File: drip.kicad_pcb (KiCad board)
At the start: 2 copper layers, 119.4 x 115.6 mm, 103 parts, among them J1 ISP, J2 2xAA Battery Holder, Q1 2n2907, Q2 2n2907, Q3 2n2907, Q4 2n2907, Q5 2n2907, Q6 2n2907, Q7 2n2907, Q8 2n2907, Q9 2n2222, SW1 Bin, SW10 Recall, SW11 D, SW12 A, SW13 7, SW14 4, SW15 1, SW16 0, SW17 Hex, SW18 E, SW19 B, SW2 Store, SW20 8, SW21 5, SW22 2, SW23 Decimal, SW24 Oct, SW25 F, SW26 C, SW27 9, SW28 6, SW29 3, SW3 Shift, SW30 +/-, SW31 Clear, SW32 K, SW33 Div, SW34 Mul, SW35 Minus, SW36 Plus, SW37 Enter, SW4 1'sCompl, SW5 Or, SW6 And, SW7 Xor, SW8 Clear Entry, SW9 Dec, U1 74HC138, U2 5641AS-4Digit-7Segment, U3 5641AS-4Digit-7Segment, U4 MSP430G2553IN20, U5 74HC251, U6 74HC138, U7 74HC595, U8 XC6372A331PR-G

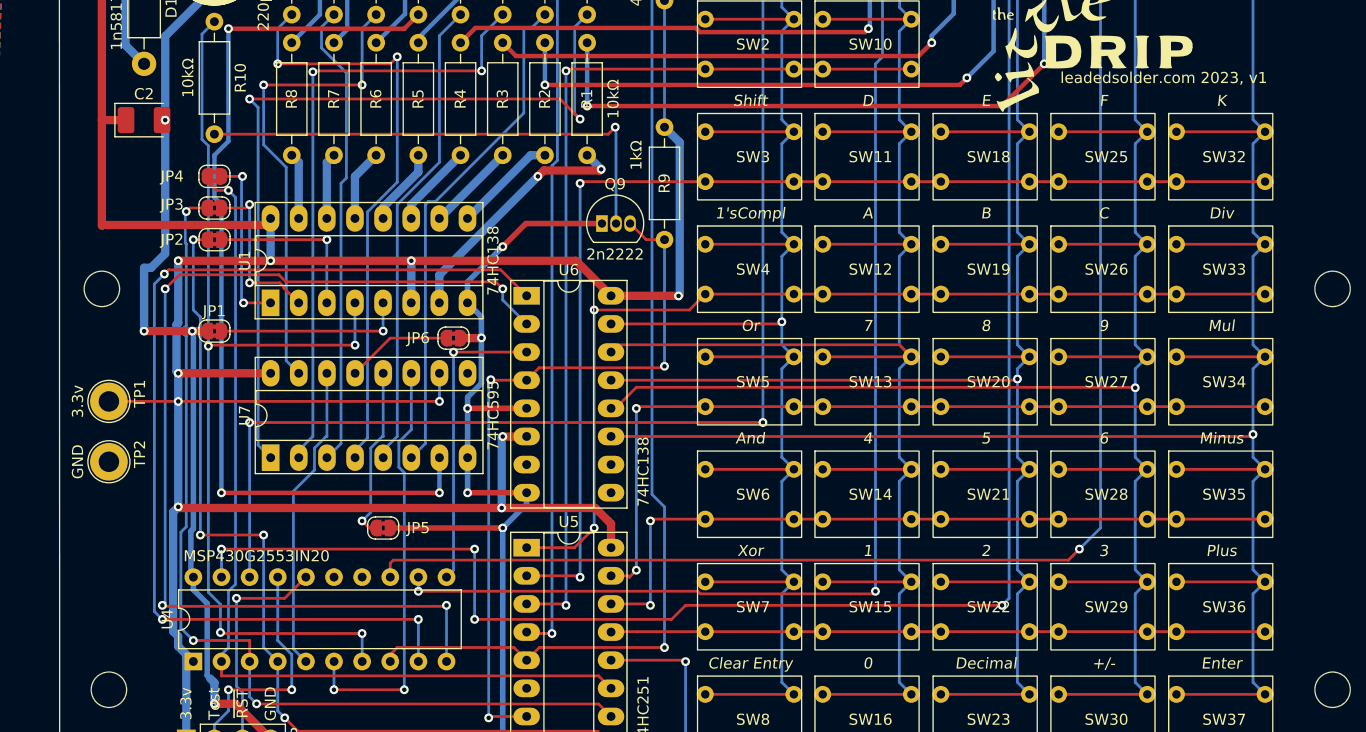
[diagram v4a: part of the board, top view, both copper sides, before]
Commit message: Reset pullup, move test hooks further apart
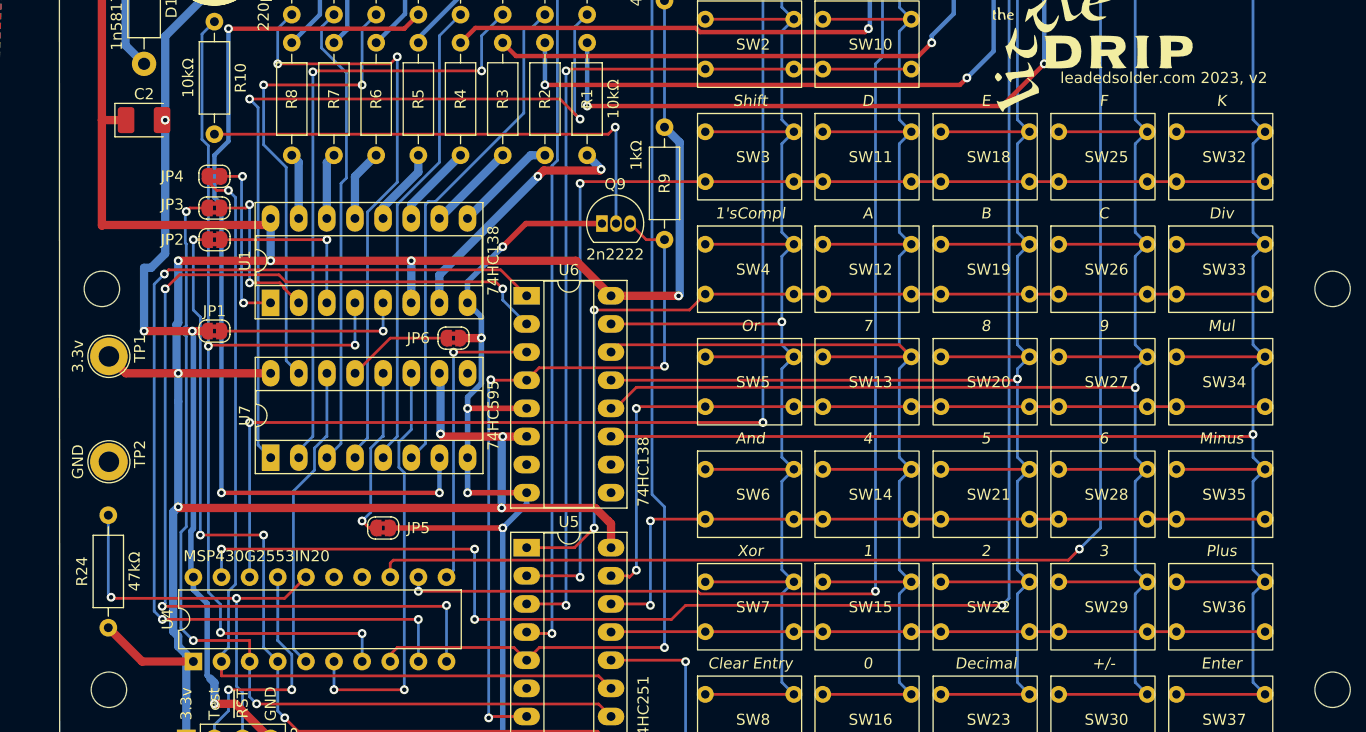
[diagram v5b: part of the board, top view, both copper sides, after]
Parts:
- added R24: 47kΩ, Resistor_THT:R_Axial_DIN0207_L6.3mm_D2.5mm_P10.16mm_Horizontal, F.Cu at (90.8, 127.8)
- moved TP1 4.06 mm to (90.8, 103.2)
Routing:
- net /~{RST}: track 20.0 -> 38.9 mm, vias 1 -> 2
- net VCC: track 288.6 -> 285.8 mm, vias 10 -> 9
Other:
- board text added: "leadedsolder.com 2023, v2"
- board text removed: "leadedsolder.com 2023, v1"

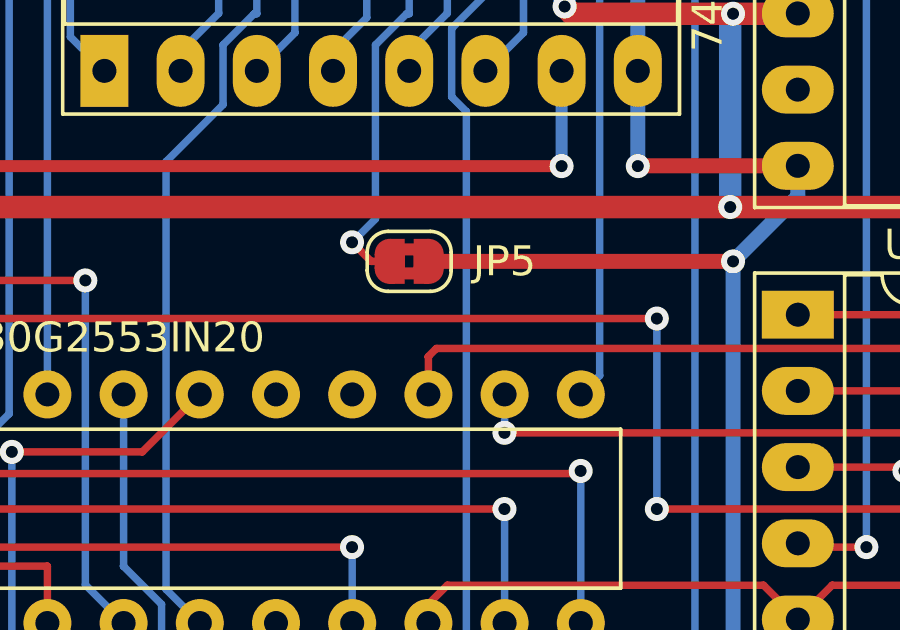
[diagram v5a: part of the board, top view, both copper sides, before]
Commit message: 7-segment working with latch bodge
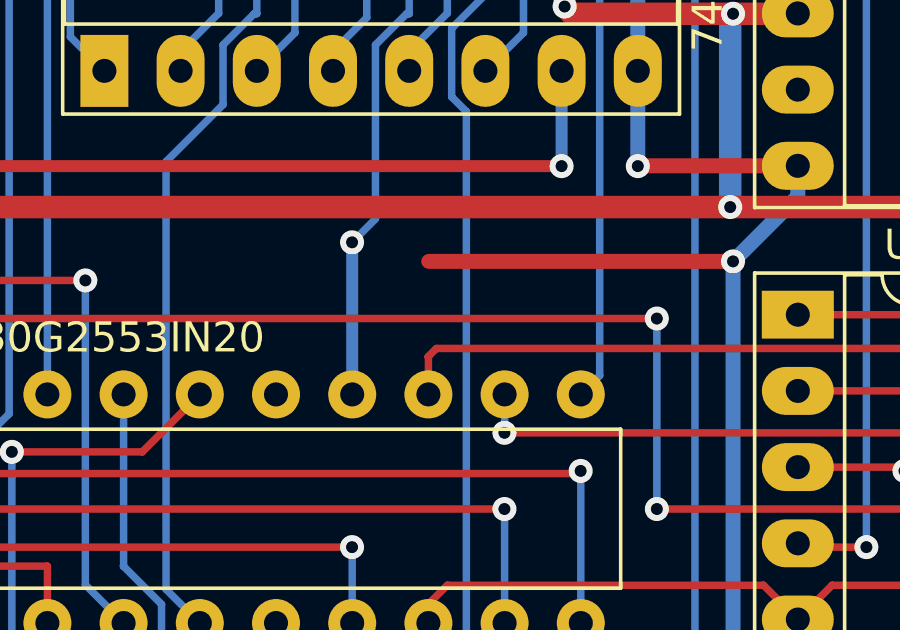
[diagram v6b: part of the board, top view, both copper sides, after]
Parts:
- removed JP5: Jumper_2_Bridged, Jumper:SolderJumper-2_P1.3mm_Bridged2Bar_RoundedPad1.0x1.5mm
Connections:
- U4 pad 14: unconnected-(U4-Pad14) -> /LED_LATCH
- U7 pad 12: Net-(JP5-Pad2) -> /LED_LATCH
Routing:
- net /LED_LATCH: track 0.00 -> 19.2 mm, vias 0 -> 1
- net Net-(JP5-Pad2): track 15.7 -> 0.00 mm, vias 1 -> 0
